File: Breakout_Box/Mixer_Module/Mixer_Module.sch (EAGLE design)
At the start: 130 parts, among them T1 2SC3324, T10 2SC3324, T11 2SC3324, T12 2SC3324, T13 2N4401, T2 2SC3324, T3 2SC3324, T4 2SC3324, T5 2SC3324, T6 2SC3324, T7 2SC3324, T8 2SC3324, T9 2SC3324, U1 OPA2209, U2 MCP10804-T

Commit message: Licenses
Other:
- note added: "Mixer Module for Nexus Project by Cycfi Research is licensed under a Creative Commons Attribution-ShareAlike 4.0 International License. Copyright CYCFI Research Inc. 2013-2016"
- note removed: "Nexus Project by Cycfi Research is licensed under a Creative Commons Attribution-NonCommercial 4.0 International License. http://creativecommons.org/licenses/by-nc/4.0/ Copyright CYCFI Research Inc. 2013-2016"
- moved on the sheet: C17, C18, C19, C20, C21, C22, C23, C24, C25, C26, C41, C42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

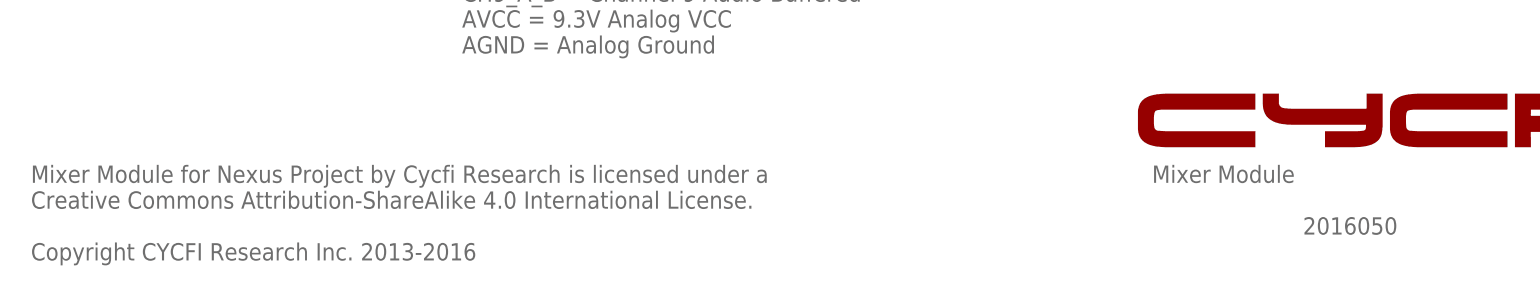
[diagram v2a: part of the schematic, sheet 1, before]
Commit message: Updated copyright and document number of schematics
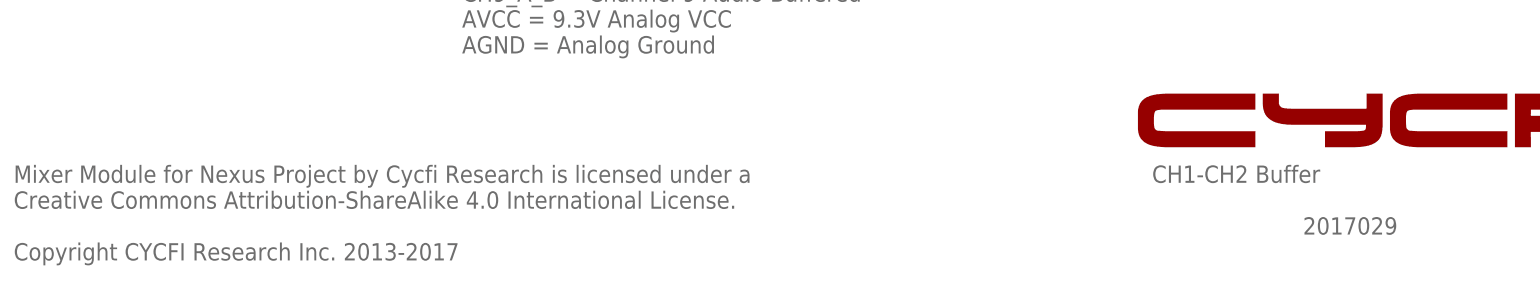
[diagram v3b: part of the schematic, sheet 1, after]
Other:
- note added: "2017029"
- note added: "CH1-CH2 Buffer"
- note added: "Mixer Module for Nexus Project by Cycfi Research is licensed under a Creative Commons Attribution-ShareAlike 4.0 International License. Copyright CYCFI Research Inc. 2013-201"
- note added: "Mixer Module for Nexus Project by Cycfi Research is licensed under a Creative Commons Attribution-ShareAlike 4.0 International License. Copyright CYCFI Research Inc. 2013-2017"
- note removed: "2016050"
- note removed: "Mixer Module"
- note removed: "Mixer Module for Nexus Project by Cycfi Research is licensed under a Creative Commons Attribution-ShareAlike 4.0 International License. Copyright CYCFI Research Inc. 2013-2016"
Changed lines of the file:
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@@
 <?xml version="1.0" encoding="utf-8"?>
 <!DOCTYPE eagle SYSTEM "eagle.dtd">
-<eagle version="6.3">
+<eagle version="7.6.0">
 <drawing>
 <settings>
@@
 <sheet>
 <plain>
-<text x="177.8" y="19.05" size="2.54" layer="95">Mixer Module</text>
+<text x="177.8" y="19.05" size="2.54" layer="95">CH1-CH2 Buffer</text>
 <text x="252.73" y="6.985" size="2.54" layer="95">v0.9</text>
-<text x="12.7" y="7.62" size="2.54" layer="95">Mixer Module for Nexus Project by Cycfi Research is licensed under a
+<text x="10.16" y="7.62" size="2.54" layer="95">Mixer Module for Nexus Project by Cycfi Research is licensed under a
 Creative Commons Attribution-ShareAlike 4.0 International License.
-Copyright CYCFI Research Inc. 2013-2016</text>
-<text x="200.025" y="11.43" size="2.54" layer="95">2016050</text>
+Copyright CYCFI Research Inc. 2013-2017</text>
+<text x="200.025" y="11.43" size="2.54" layer="95">2017029</text>
 <wire x1="124.46" y1="152.4" x2="124.46" y2="142.24" width="0.1524" layer="94" style="shortdash"/>
 <wire x1="124.46" y1="142.24" x2="119.38" y2="142.24" width="0.1524" layer="94" style="shortdash"/>
@@
 <text x="177.8" y="19.05" size="2.54" layer="95">CH3-CH7 Buffer</text>
 <text x="252.73" y="6.985" size="2.54" layer="95">v0.9</text>
-<text x="200.025" y="11.43" size="2.54" layer="95">2016050</text>
+<text x="200.025" y="11.43" size="2.54" layer="95">2017029</text>
 <wire x1="45.72" y1="161.6075" x2="45.72" y2="158.4325" width="0.1524" layer="95"/>
 <wire x1="45.72" y1="158.4325" x2="52.07" y2="158.4325" width="0.1524" layer="95"/>
@@
 <text x="457.2" y="19.05" size="2.54" layer="95">CH8-CH12_A Buffer</text>
 <text x="532.13" y="6.985" size="2.54" layer="95">v0.9</text>
-<text x="479.425" y="11.43" size="2.54" layer="95">2016050</text>
+<text x="479.425" y="11.43" size="2.54" layer="95">2017029</text>
 <wire x1="327.66" y1="161.6075" x2="327.66" y2="158.4325" width="0.1524" layer="95"/>
 <wire x1="327.66" y1="158.4325" x2="334.01" y2="158.4325" width="0.1524" layer="95"/>
@@
 <text x="285.75" y="6.35" size="2.54" layer="95">Mixer Module for Nexus Project by Cycfi Research is licensed under a
 Creative Commons Attribution-ShareAlike 4.0 International License.
-Copyright CYCFI Research Inc. 2013-2016</text>
+Copyright CYCFI Research Inc. 2013-2017</text>
 <text x="7.62" y="7.62" size="2.54" layer="95">Mixer Module for Nexus Project by Cycfi Research is licensed under a
 Creative Commons Attribution-ShareAlike 4.0 International License.
-Copyright CYCFI Research Inc. 2013-2016</text>
+Copyright CYCFI Research Inc. 2013-2017</text>
 <rectangle x1="179.80469375" y1="24.29065625" x2="193.0330125" y2="24.29954375" layer="94"/>
 <rectangle x1="203.283184375" y1="24.29065625" x2="207.683734375" y2="24.29954375" layer="94"/>
@@
 AGND = Analog Ground</text>
 <text x="252.73" y="6.985" size="2.54" layer="95">v0.92</text>
-<text x="12.7" y="12.7" size="2.54" layer="95">Mixer Module for Nexus Project by Cycfi Research is licensed under a
+<text x="7.62" y="12.7" size="2.54" layer="95">Mixer Module for Nexus Project by Cycfi Research is licensed under a
 Creative Commons Attribution-ShareAlike 4.0 International License.
-Copyright CYCFI Research Inc. 2013-2016</text>
-<text x="200.025" y="11.43" size="2.54" layer="95">2016050</text>
+Copyright CYCFI Research Inc. 2013-201</text>
+<text x="200.025" y="11.43" size="2.54" layer="95">2017029</text>
 <wire x1="185.42" y1="116.205" x2="183.8325" y2="117.7925" width="0.254" layer="95"/>
 <wire x1="183.8325" y1="117.7925" x2="173.99" y2="117.7925" width="0.254" layer="95"/>
@@
 <text x="35.56" y="53.34" size="2.54" layer="95">Expansion Headers</text>
 <text x="252.73" y="6.985" size="2.54" layer="95">v0.9</text>
-<text x="200.025" y="8.89" size="2.54" layer="95">2016050</text>
+<text x="202.565" y="11.43" size="2.54" layer="95">2017029</text>
 <text x="8.89" y="125.73" size="1.778" layer="95">CH9_CV</text>
 <text x="8.89" y="123.19" size="1.778" layer="95">CH10_CV</text>
@@
 <text x="10.16" y="6.35" size="2.54" layer="95">Mixer Module for Nexus Project by Cycfi Research is licensed under a
 Creative Commons Attribution-ShareAlike 4.0 International License.
-Copyright CYCFI Research Inc. 2013-2016</text>
+Copyright CYCFI Research Inc. 2013-2017</text>
 <wire x1="162.56" y1="35.56" x2="113.03" y2="35.56" width="0.1524" layer="94" style="longdash"/>
 <wire x1="113.03" y1="35.56" x2="0" y2="35.56" width="0.1524" layer="94" style="longdash"/>
